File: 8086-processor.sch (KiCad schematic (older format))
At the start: 19 parts

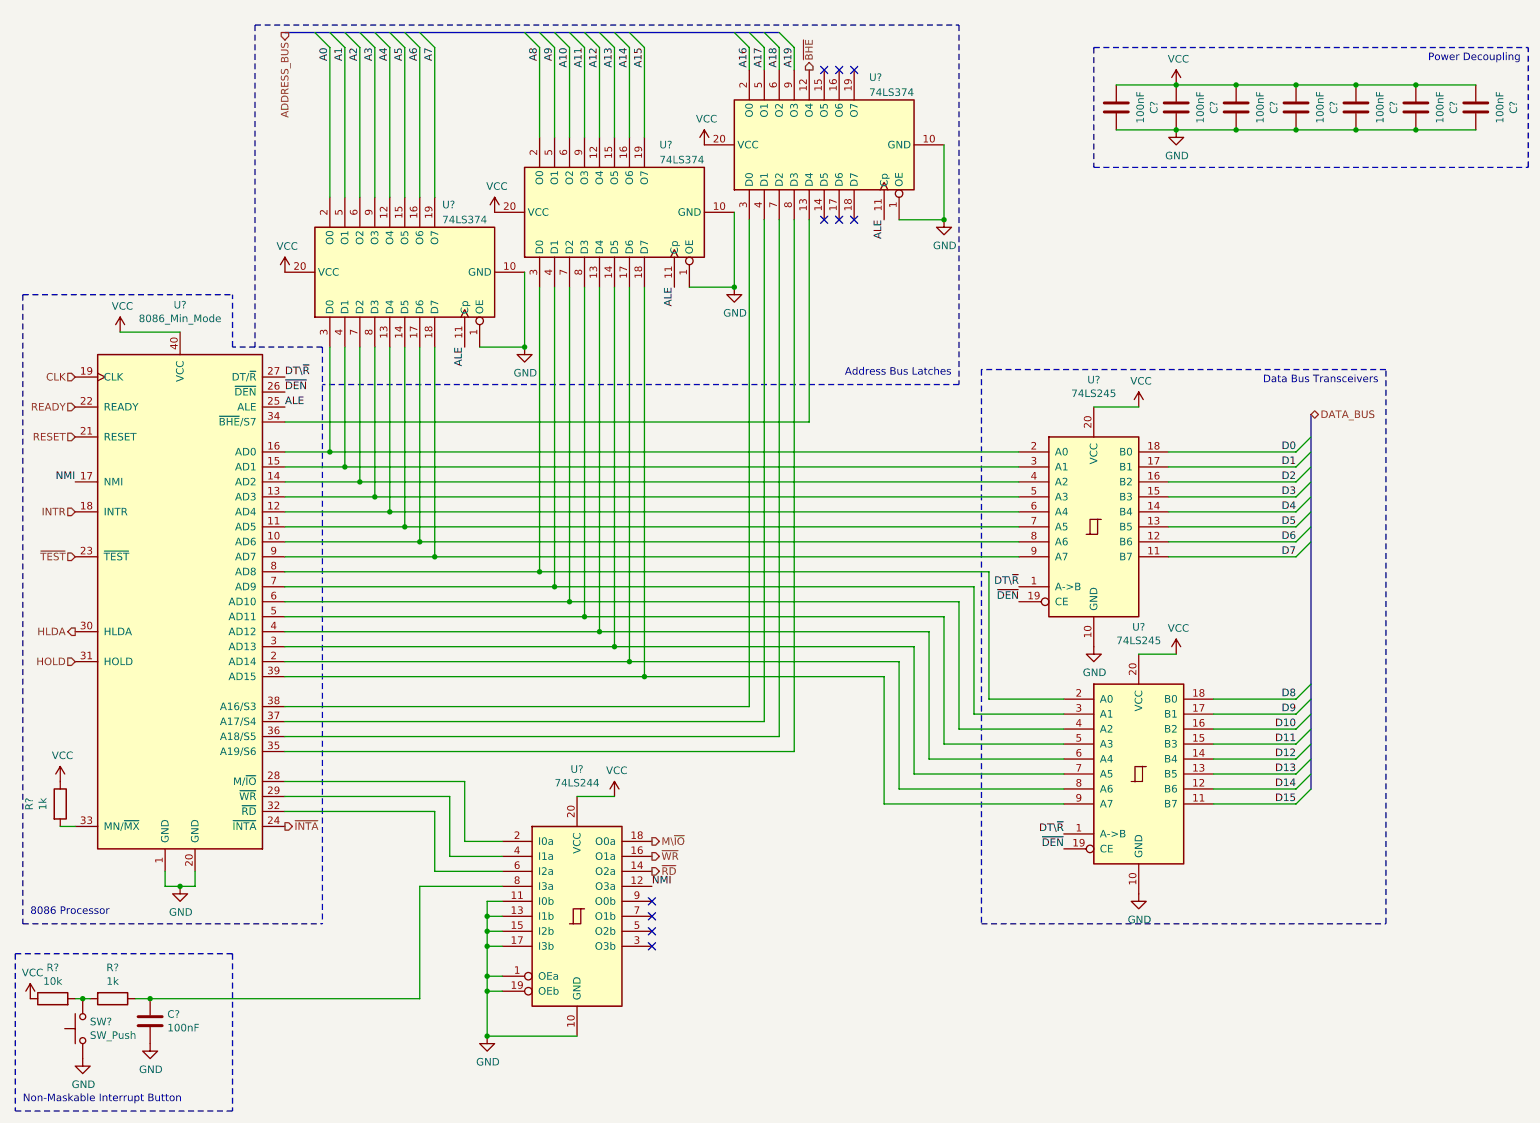
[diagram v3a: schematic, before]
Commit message: General edits; removed floating inputs
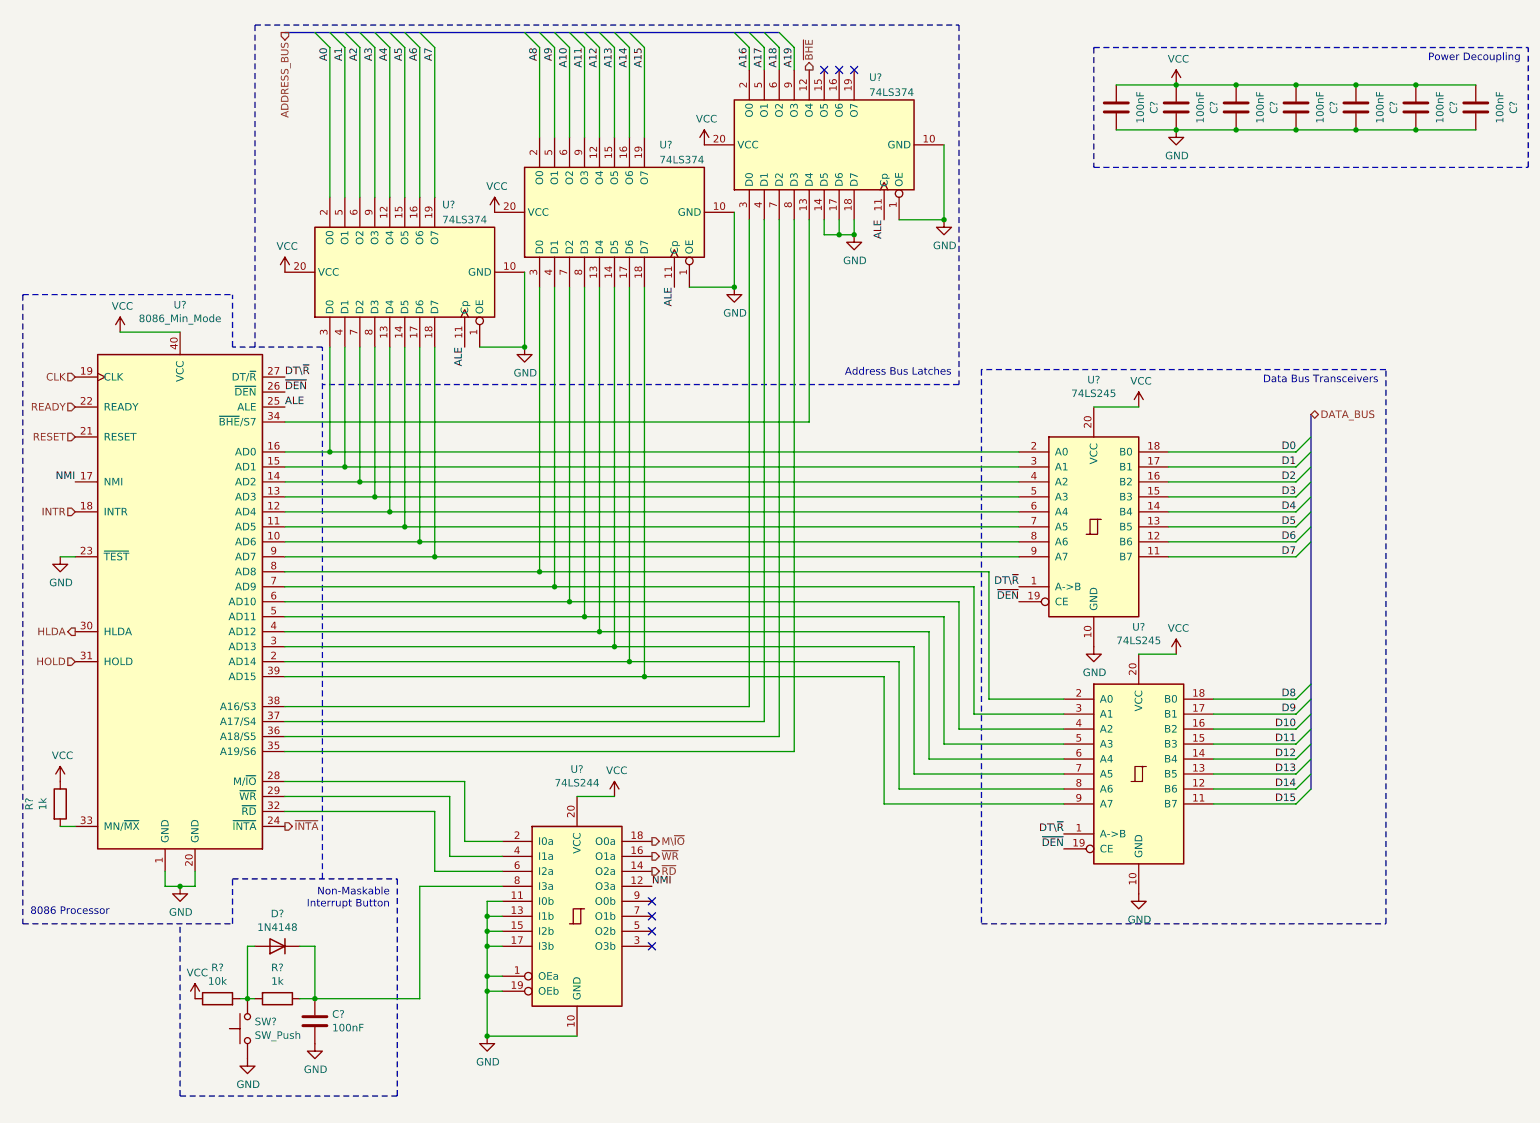
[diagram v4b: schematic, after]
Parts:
- added D?: 1N4148, Diode_THT:D_DO-35_SOD27_P7.62mm_Horizontal, symbol Diode:1N4148
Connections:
- net ~TEST is gone; now on net GND: U?.23 (~TEST~)
- net GND: now also U?.14 (D5), U?.17 (D6), U?.18 (D7)
- net at C?.1, R?.1, U?.8 (I3a): now also D?.1 (K)
- net at R?.2, R?.2, SW?.2: now also D?.2 (A)
- no-connect marks 10 -> 7
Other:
- note added: "Non-Maskable\nInterrupt Button"
- note removed: "Non-Maskable Interrupt Button"
- moved on the sheet: C?, R?, SW?
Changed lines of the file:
@@
 $Descr A4 11693 8268
 encoding utf-8
-Sheet 13 15
+Sheet 12 15
 Title "8086-processor"
 Date ""
@@
 Text Label 6500 1800 3    50   ~ 0
 ALE
-NoConn ~ 6100 1800
-NoConn ~ 6200 1800
-NoConn ~ 6300 1800
 NoConn ~ 6300 800
 NoConn ~ 6200 800
@@
 Text HLabel 1100 3050 0    50   Input ~ 0
 READY
-Text HLabel 1100 4050 0    50   Input ~ 0
-~TEST
 Text HLabel 1100 4750 0    50   Input ~ 0
 HOLD
@@
 	750  2300 750  6500
 Wire Notes Line
-	750  6500 2750 6500
-Wire Notes Line
 	2750 2650 2150 2650
 Wire Notes Line
@@
 Wire Notes Line
 	2300 500  2300 2650
-Wire Notes Line
-	2750 2650 2750 6500
 Wire Notes Line
 	7000 2900 2750 2900
@@
 Text Notes 10750 750  2    50   ~ 0
 Power Decoupling
-Connection ~ 1600 7000
-Wire Wire Line
-	1500 7000 1600 7000
-Wire Wire Line
-	1150 7000 1100 7000
-Connection ~ 1150 7000
-Wire Wire Line
-	1200 7000 1150 7000
+Connection ~ 2700 7000
+Wire Wire Line
+	2600 7000 2700 7000
+Wire Wire Line
+	2250 7000 2200 7000
+Connection ~ 2250 7000
+Wire Wire Line
+	2300 7000 2250 7000
 $Comp
 L power:GND #PWR?
 U 1 1 627AC8BB
-P 1600 7300
-F 0 "#PWR?" H 1600 7050 50  0001 C CNN
-F 1 "GND" H 1605 7127 50  0000 C CNN
-F 2 "" H 1600 7300 50  0001 C CNN
-F 3 "" H 1600 7300 50  0001 C CNN
-	1    1600 7300
+P 2700 7300
+F 0 "#PWR?" H 2700 7050 50  0001 C CNN
+F 1 "GND" H 2705 7127 50  0000 C CNN
+F 2 "" H 2700 7300 50  0001 C CNN
+F 3 "" H 2700 7300 50  0001 C CNN
+	1    2700 7300
 	1    0    0    -1
 $EndComp
@@
 L Device:R R?
 U 1 1 6279446B
-P 1350 7000
-F 0 "R?" V 1143 7000 50  0000 C CNN
-F 1 "1k" V 1234 7000 50  0000 C CNN
-F 2 "" V 1280 7000 50  0001 C CNN
-F 3 "~" H 1350 7000 50  0001 C CNN
-	1    1350 7000
+P 2450 7000
+F 0 "R?" V 2243 7000 50  0000 C CNN
+F 1 "1k" V 2334 7000 50  0000 C CNN
+F 2 "" V 2380 7000 50  0001 C CNN
+F 3 "~" H 2450 7000 50  0001 C CNN
+	1    2450 7000
 	0    1    1    0
 $EndComp
@@
 L power:VCC #PWR?
 U 1 1 6278DB4C
-P 800 7000
-F 0 "#PWR?" H 800 6850 50  0001 C CNN
-F 1 "VCC" H 815 7173 50  0000 C CNN
-F 2 "" H 800 7000 50  0001 C CNN
-F 3 "" H 800 7000 50  0001 C CNN
-	1    800  7000
+P 1900 7000
+F 0 "#PWR?" H 1900 6850 50  0001 C CNN
+F 1 "VCC" H 1915 7173 50  0000 C CNN
+F 2 "" H 1900 7000 50  0001 C CNN
+F 3 "" H 1900 7000 50  0001 C CNN
+	1    1900 7000
 	1    0    0    -1
 $EndComp
@@
 L Device:C C?
 U 1 1 6277FDCA
-P 1600 7150
-F 0 "C?" H 1715 7196 50  0000 L CNN
-F 1 "100nF" H 1715 7105 50  0000 L CNN
-F 2 "" H 1638 7000 50  0001 C CNN
-F 3 "~" H 1600 7150 50  0001 C CNN
-	1    1600 7150
+P 2700 7150
+F 0 "C?" H 2815 7196 50  0000 L CNN
+F 1 "100nF" H 2815 7105 50  0000 L CNN
+F 2 "" H 2738 7000 50  0001 C CNN
+F 3 "~" H 2700 7150 50  0001 C CNN
+	1    2700 7150
 	1    0    0    -1
 $EndComp
@@
 L Device:R R?
 U 1 1 6277EAFF
-P 950 7000
-F 0 "R?" V 1157 7000 50  0000 C CNN
-F 1 "10k" V 1066 7000 50  0000 C CNN
-F 2 "" V 880 7000 50  0001 C CNN
-F 3 "~" H 950 7000 50  0001 C CNN
-	1    950  7000
+P 2050 7000
+F 0 "R?" V 2257 7000 50  0000 C CNN
+F 1 "10k" V 2166 7000 50  0000 C CNN
+F 2 "" V 1980 7000 50  0001 C CNN
+F 3 "~" H 2050 7000 50  0001 C CNN
+	1    2050 7000
 	0    -1   -1   0
 $EndComp
@@
 L Switch:SW_Push SW?
 U 1 1 626B0BE8
-P 1150 7200
-F 0 "SW?" V 1196 7152 50  0000 R CNN
-F 1 "SW_Push" V 1105 7152 50  0000 R CNN
-F 2 "" H 1150 7400 50  0001 C CNN
-F 3 "~" H 1150 7400 50  0001 C CNN
-	1    1150 7200
+P 2250 7200
+F 0 "SW?" V 2296 7152 50  0000 R CNN
+F 1 "SW_Push" V 2205 7152 50  0000 R CNN
+F 2 "" H 2250 7400 50  0001 C CNN
+F 3 "~" H 2250 7400 50  0001 C CNN
+	1    2250 7200
 	0    -1   -1   0
 $EndComp
-Text Notes 750  7700 0    50   ~ 0
-Non-Maskable Interrupt Button
+Text Notes 3200 6400 2    50   ~ 0
+Non-Maskable\nInterrupt Button
 Text Label 4950 6250 0    50   ~ 0
 NMI
@@
 L power:GND #PWR?
 U 1 1 6233B1ED
-P 1150 7400
-F 0 "#PWR?" H 1150 7150 50  0001 C CNN
-F 1 "GND" H 1155 7227 50  0000 C CNN
-F 2 "" H 1150 7400 50  0001 C CNN
-F 3 "" H 1150 7400 50  0001 C CNN
-	1    1150 7400
+P 2250 7400
+F 0 "#PWR?" H 2250 7150 50  0001 C CNN
+F 1 "GND" H 2255 7227 50  0000 C CNN
+F 2 "" H 2250 7400 50  0001 C CNN
+F 3 "" H 2250 7400 50  0001 C CNN
+	1    2250 7400
 	1    0    0    -1
 $EndComp
@@
 Wire Notes Line
 	7900 650  10800 650
-Wire Notes Line
-	700  6700 700  7750
-Wire Notes Line
-	2150 6700 2150 7750
-Wire Notes Line
-	700  6700 2150 6700
-Wire Notes Line
-	700  7750 2150 7750
 Wire Wire Line
 	3400 7000 3400 6250
@@
 	3400 6250 3950 6250
 Wire Wire Line
-	1600 7000 3400 7000
+	2700 7000 3400 7000
 Wire Notes Line
 	7900 650  7900 1450
@@
 Wire Notes Line
 	10800 1450 10800 650
+$Comp
+L Diode:1N4148 D?
+U 1 1 61F82EF7
+P 2450 6650
+AR Path="/61CB92C1/61F82EF7" Ref="D?"  Part="1"
+AR Path="/6190420C/61F82EF7" Ref="D?"  Part="1"
+F 0 "D?" H 2450 6433 50  0000 C CNN
+F 1 "1N4148" H 2450 6524 50  0000 C CNN
+F 2 "Diode_THT:D_DO-35_SOD27_P7.62mm_Horizontal" H 2450 6475 50  0001 C CNN
+F 3 "https://assets.nexperia.com/documents/data-sheet/1N4148_1N4448.pdf" H 2450 6650 50  0001 C CNN
+	1    2450 6650
+	-1   0    0    1
+$EndComp
+Wire Notes Line
+	2150 6500 2150 6200
+Wire Notes Line
+	750  6500 2150 6500
+Wire Notes Line
+	2750 6200 2750 2650
+Wire Notes Line
+	2150 6200 3250 6200
+Wire Notes Line
+	1800 7650 3250 7650
+Wire Notes Line
+	1800 7650 1800 6500
+Wire Notes Line
+	3250 7650 3250 6200
+Wire Wire Line
+	2600 6650 2700 6650
+Wire Wire Line
+	2300 6650 2250 6650
+Wire Wire Line
+	2250 6650 2250 7000
+Wire Wire Line
+	2700 6650 2700 7000
+Wire Wire Line
+	1100 4050 1000 4050
+$Comp
+L power:GND #PWR?
+U 1 1 6203EB57
+P 1000 4050
+F 0 "#PWR?" H 1000 3800 50  0001 C CNN
+F 1 "GND" H 1005 3877 50  0000 C CNN
+F 2 "" H 1000 4050 50  0001 C CNN
+F 3 "" H 1000 4050 50  0001 C CNN
+	1    1000 4050
+	1    0    0    -1
+$EndComp
+Wire Wire Line
+	6100 1800 6100 1900
+Wire Wire Line
+	6100 1900 6200 1900
+Wire Wire Line
+	6200 1900 6200 1800
+Wire Wire Line
+	6200 1900 6300 1900
+Wire Wire Line
+	6300 1900 6300 1800
 Wire Bus Line
 	9350 3100 9350 5600
 Wire Bus Line
 	2500 550  5800 550
+Connection ~ 6200 1900
+$Comp
+L power:GND #PWR?
+U 1 1 6213CD02
+P 6300 1900
+F 0 "#PWR?" H 6300 1650 50  0001 C CNN
+F 1 "GND" H 6305 1727 50  0000 C CNN
+F 2 "" H 6300 1900 50  0001 C CNN
+F 3 "" H 6300 1900 50  0001 C CNN
+	1    6300 1900
+	1    0    0    -1
+$EndComp
+Connection ~ 6300 1900
 $EndSCHEMATC

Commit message: Updates to pass ERC
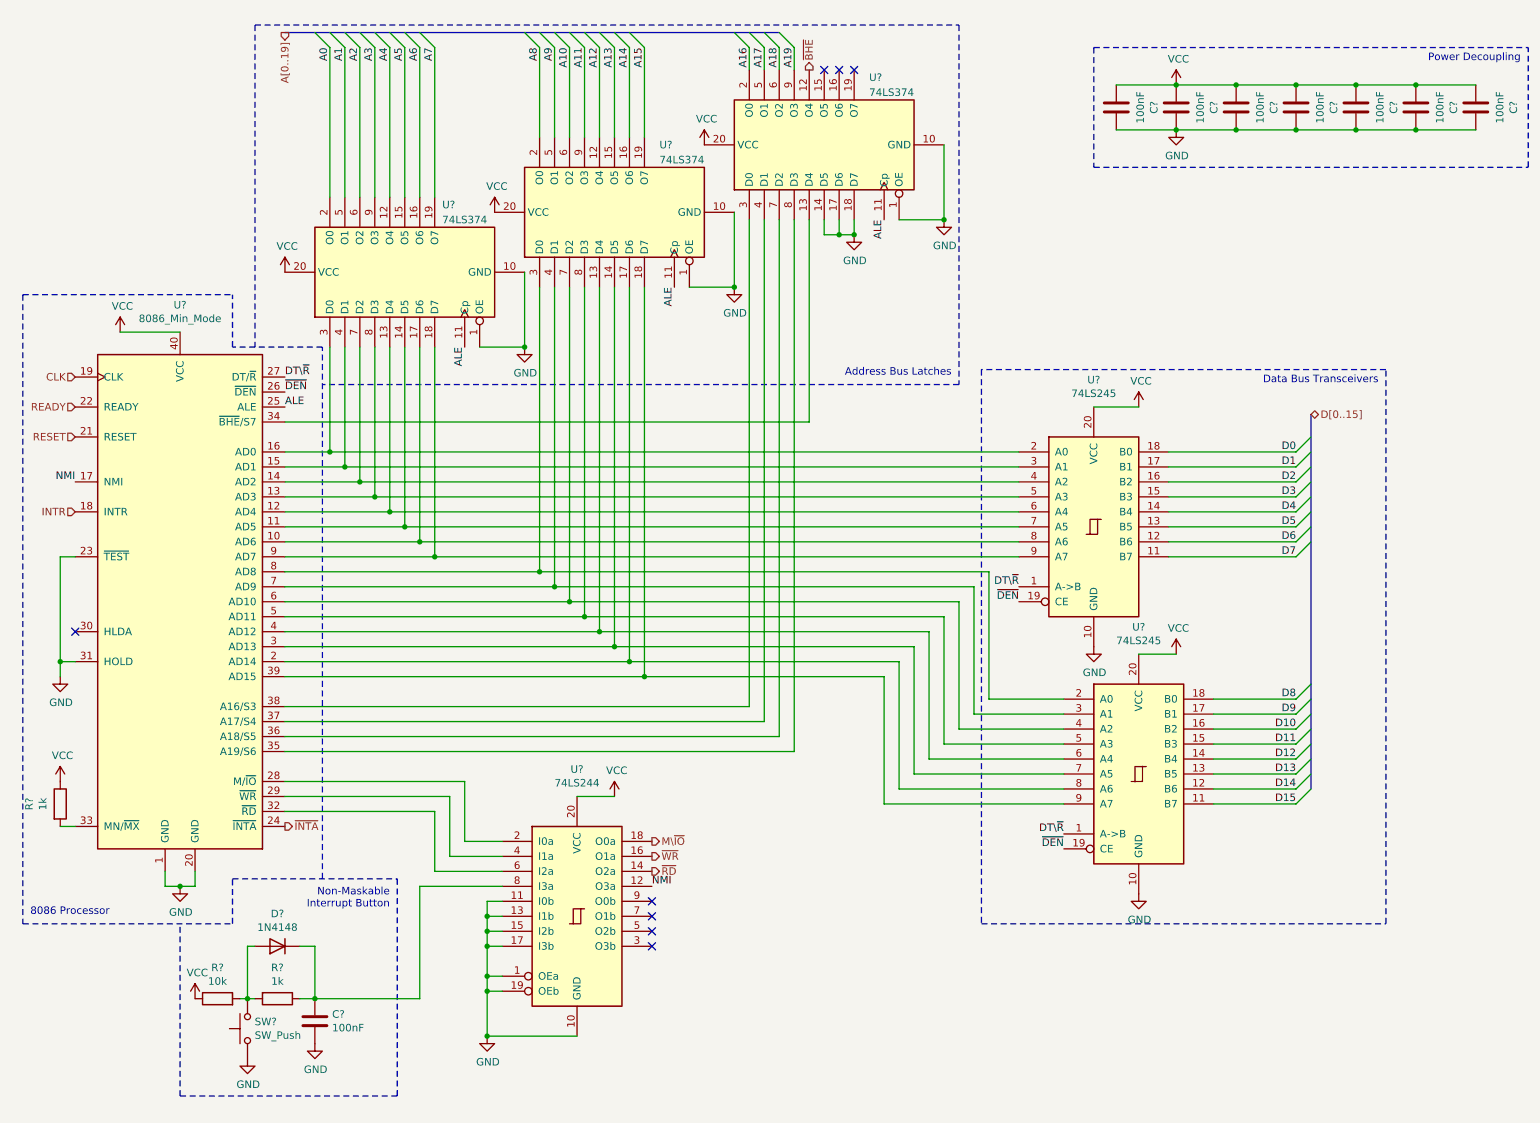
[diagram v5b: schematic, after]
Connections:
- net HOLD is gone; now on net GND: U?.31 (HOLD)
- net HLDA: no longer names the net of U?.30 (HLDA)
- no-connect marks 7 -> 8
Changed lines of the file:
@@
 CLK
 Text HLabel 2500 550  3    50   Output ~ 0
-ADDRESS_BUS
+A[0..19]
 Text HLabel 6000 800  1    50   Output ~ 0
 ~BHE
 Text HLabel 9350 3100 2    50   BiDi ~ 0
-DATA_BUS
+D[0..15]
 Text HLabel 1100 3750 0    50   Input ~ 0
 INTR
@@
 Text HLabel 1100 3050 0    50   Input ~ 0
 READY
-Text HLabel 1100 4750 0    50   Input ~ 0
-HOLD
-Text HLabel 1100 4550 0    50   Output ~ 0
-HLDA
 Text HLabel 2500 5850 2    50   Output ~ 0
 ~INTA
@@
 L power:GND #PWR?
 U 1 1 6203EB57
-P 1000 4050
-F 0 "#PWR?" H 1000 3800 50  0001 C CNN
-F 1 "GND" H 1005 3877 50  0000 C CNN
-F 2 "" H 1000 4050 50  0001 C CNN
-F 3 "" H 1000 4050 50  0001 C CNN
-	1    1000 4050
+P 1000 4850
+F 0 "#PWR?" H 1000 4600 50  0001 C CNN
+F 1 "GND" H 1005 4677 50  0000 C CNN
+F 2 "" H 1000 4850 50  0001 C CNN
+F 3 "" H 1000 4850 50  0001 C CNN
+	1    1000 4850
 	1    0    0    -1
 $EndComp
@@
 Wire Wire Line
 	6300 1900 6300 1800
-Wire Bus Line
-	9350 3100 9350 5600
-Wire Bus Line
-	2500 550  5800 550
 Connection ~ 6200 1900
 $Comp
@@
 $EndComp
 Connection ~ 6300 1900
+Wire Wire Line
+	1000 4050 1000 4750
+Wire Wire Line
+	1100 4750 1000 4750
+Connection ~ 1000 4750
+Wire Wire Line
+	1000 4850 1000 4750
+NoConn ~ 1100 4550
+Wire Bus Line
+	9350 3100 9350 5600
+Wire Bus Line
+	2500 550  5800 550
 $EndSCHEMATC
